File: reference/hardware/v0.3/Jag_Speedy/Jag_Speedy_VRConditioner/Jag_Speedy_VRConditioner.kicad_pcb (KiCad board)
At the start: 2 copper layers, 15 parts, among them IC1 MAX9926UAEE+, J1 Conn_02x04_Counter_Clockwise

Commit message: VR PCB
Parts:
- moved C1 14.9 mm to (149.9, 83.8), turned to 90 degrees
- moved R4 6.02 mm to (144.8, 83.8), turned to 90 degrees
- moved R7 2.21 mm to (141.0, 83.8), turned to 90 degrees
- turned R3 to 270 degrees
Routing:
- net Net-(C1-Pad2): track 36.7 -> 22.3 mm
- net Net-(C1-Pad1): track 24.5 -> 11.3 mm
- net VR1+: track 9.36 -> 18.2 mm
- net VR1-: track 9.19 -> 17.1 mm

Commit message: VR Cond PCB update
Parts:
- J1: value Conn_02x04_Counter_Clockwise -> Conn; moved to B.Cu
- moved C2 26.1 mm to (151.1, 82.9), turned to 90 degrees
- moved R5 20.4 mm to (146.1, 82.9), turned to 270 degrees
- moved R6 19.7 mm to (148.6, 82.9), turned to 90 degrees
- moved R8 18.9 mm to (135.9, 82.9), turned to 90 degrees
- moved C5 18.0 mm to (133.3, 96.9), turned to 90 degrees
- moved R2 15.8 mm to (143.5, 96.9), turned to 270 degrees
- moved C4 14.3 mm to (135.9, 96.9), turned to 90 degrees
- moved R1 14.1 mm to (141.0, 96.9), turned to 270 degrees
- moved R4 11.5 mm to (133.3, 82.9)
- moved C3 11.1 mm to (138.4, 96.9), turned to 90 degrees
- moved IC1 10.4 mm to (148.6, 90.2), turned to 90 degrees
- moved C1 6.42 mm to (143.5, 82.9)
- moved R3 6.09 mm to (141.0, 82.9)
- moved R7 2.71 mm to (138.4, 82.9)
- moved J1 1.98 mm to (134.6, 88.9), turned to 270 degrees
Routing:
- net Ground: track 22.7 -> 56.8 mm
- net VR2-: track 24.3 -> 46.3 mm, vias 0 -> 2
- net VR2+: track 4.66 -> 20.6 mm, vias 0 -> 1
- net Output1: track 35.1 -> 22.5 mm
- net Net-(C2-Pad1): track 0.00 -> 9.84 mm
- net Net-(C2-Pad2): track 0.00 -> 9.09 mm
- net VR1-: track 17.1 -> 10.7 mm, vias 0 -> 2
- net Net-(C1-Pad2): track 22.3 -> 18.1 mm
- net VR1+: track 18.2 -> 22.1 mm
- net 5V: track 32.9 -> 36.5 mm, vias 0 -> 1
- net Net-(C1-Pad1): track 11.3 -> 8.26 mm
- net Output2: track 16.7 -> 15.2 mm
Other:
- net class Power added: clearance 0.3, trace_width 0.25, via_dia 0.8, via_drill 0.4
- board text added: "FiP"

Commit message: PCB Update
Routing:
- net Ground: track 56.8 -> 47.5 mm, vias 0 -> 1
- net VR1+: track 22.1 -> 15.1 mm, vias 0 -> 1
- net VR2-: track 46.3 -> 39.5 mm
- net VR1-: track 10.7 -> 12.3 mm, vias 2 -> 1

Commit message: VR PCB Update
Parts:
- C3, C4, C5, R1, R2: moved to B.Cu
- R7, R8: footprint Resistor_SMD:R_0805_2012Metric -> Resistor_THT:R_Axial_DIN0414_L11.9mm_D4.5mm_P15.24mm_Horizontal
- moved R7 23.2 mm to (156.2, 97.8)
- moved R5 12.7 mm to (133.3, 82.9)
- moved R6 11.7 mm to (136.9, 82.9)
- moved R4 10.7 mm to (144.0, 82.9)
- moved R8 8.90 mm to (127.0, 82.5), turned to 270 degrees
- moved R2 6.48 mm to (149.9, 98.1), turned to 90 degrees
- moved R1 4.62 mm to (145.4, 98.1), turned to 90 degrees
- moved C1 4.06 mm to (147.6, 82.9), turned to 270 degrees
- moved C3 2.84 mm to (141.0, 98.1), turned to 270 degrees
- moved C5 1.80 mm to (132.1, 98.1), turned to 270 degrees
- moved C4 1.42 mm to (136.5, 98.1), turned to 270 degrees
- moved R3 0.51 mm to (140.5, 82.9)
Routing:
- net 5V: track 36.4 -> 61.9 mm
- net VR1+: track 15.1 -> 35.8 mm
- net VR1-: track 12.3 -> 32.7 mm
- net Ground: track 47.5 -> 67.1 mm
- net Net-(C2-Pad1): track 9.84 -> 28.4 mm
- net Net-(C2-Pad2): track 9.09 -> 25.3 mm, vias 0 -> 2
- net VR2-: track 39.5 -> 26.7 mm, vias 2 -> 0
- net Net-(C1-Pad2): track 18.1 -> 11.8 mm
- net Output1: track 22.5 -> 16.4 mm, vias 0 -> 1
- net Net-(C1-Pad1): track 8.26 -> 13.6 mm
- net VR2+: track 20.6 -> 16.4 mm
- net Output2: track 15.2 -> 17.7 mm, vias 0 -> 1

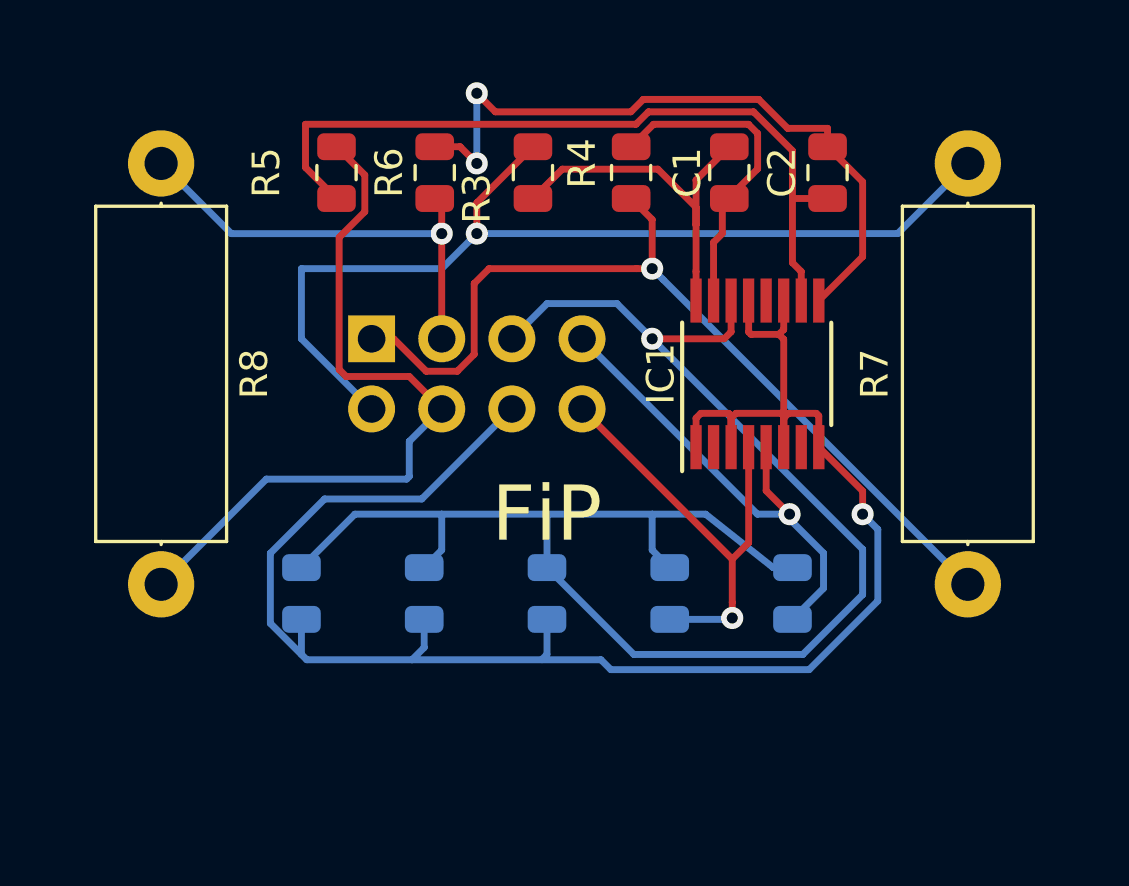
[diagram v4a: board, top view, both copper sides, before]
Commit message: Ground & Pwer Planes
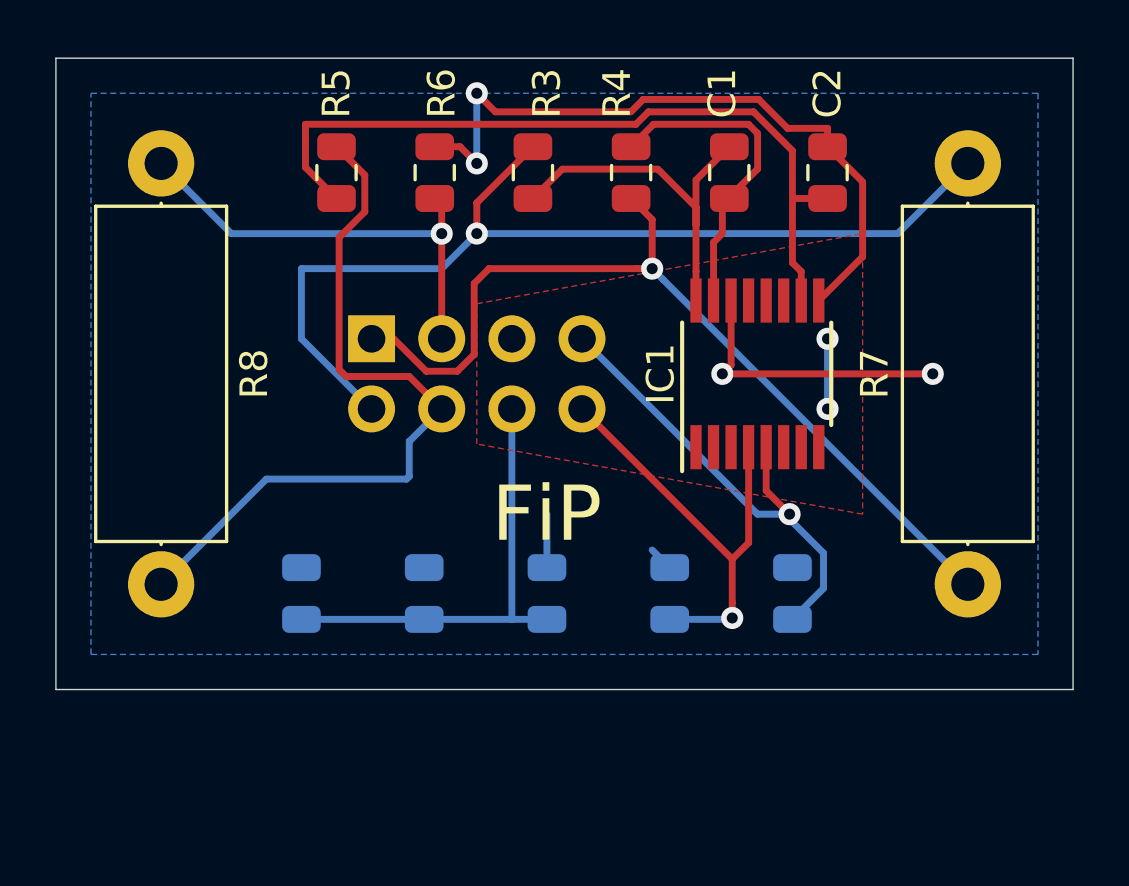
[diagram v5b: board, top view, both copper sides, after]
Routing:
- net 5V: track 61.9 -> 13.2 mm, vias 1 -> 2
- net Ground: track 67.1 -> 19.0 mm, vias 1 -> 2
- added copper zone on B.Cu, net 5V
- added copper zone on F.Cu, net Ground
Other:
- board outline added: 36.8 x 22.9 mm
- net class Power: clearance 0.3 -> 0.2
- net class Signal added: clearance 0.1, trace_width 0.2, via_dia 0.6, via_drill 0.4

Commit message: PCB Connector Fix
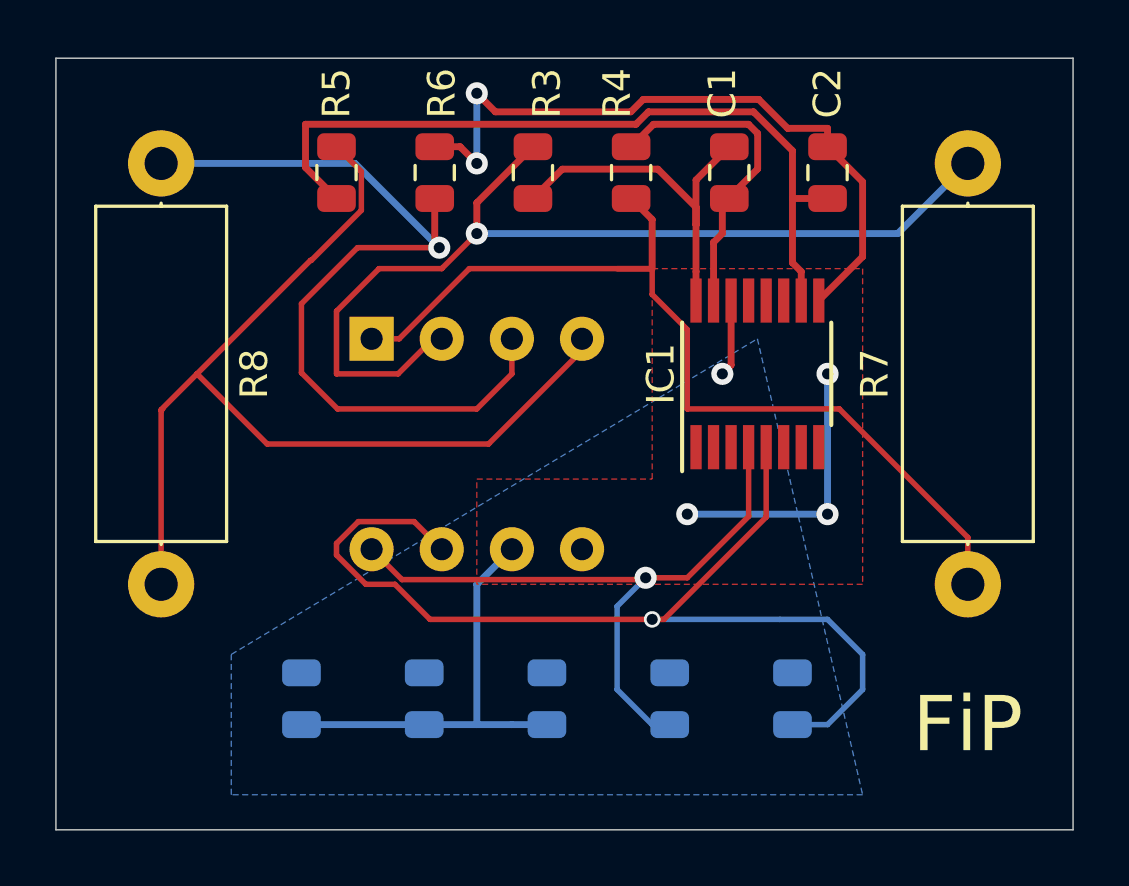
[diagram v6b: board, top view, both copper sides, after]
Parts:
- J1: footprint Connector_PinHeader_2.54mm:PinHeader_2x04_P2.54mm_Vertical -> Package_DIP:DIP-8_W7.62mm_Socket
- moved C3 3.81 mm to (141.0, 101.9)
- moved C4 3.81 mm to (136.5, 101.9)
- moved C5 3.81 mm to (132.1, 101.9)
- moved R1 3.81 mm to (145.4, 101.9)
- moved R2 3.81 mm to (149.9, 101.9)
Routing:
- net Output2: track 17.7 -> 38.0 mm
- net VR2+: track 16.4 -> 31.5 mm
- net 5V: track 13.2 -> 2.79 mm, vias 2 -> 1
- net VR2-: track 26.7 -> 36.2 mm
- net Output1: track 16.4 -> 24.5 mm
- net Ground: track 19.0 -> 25.9 mm, vias 2 -> 3
- net VR1-: track 32.7 -> 34.7 mm, vias 1 -> 0
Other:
- board size 36.8 x 22.9 mm -> 36.8 x 27.9 mm

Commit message: PCB Changes
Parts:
- moved C5 25.0 mm to (156.2, 95.2), turned to 180 degrees
- moved C4 21.7 mm to (156.2, 92.7), turned to 180 degrees
- moved C3 19.3 mm to (156.2, 90.2), turned to 180 degrees
- moved R2 18.0 mm to (156.2, 85.1), turned to 0 degrees
- moved R1 17.9 mm to (156.2, 87.6), turned to 0 degrees
- moved R8 1.27 mm to (128.3, 82.5)
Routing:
- net Output1: track 24.5 -> 45.2 mm
- net Output2: track 38.0 -> 48.5 mm
- net Ground: track 25.9 -> 16.8 mm
- net VR2+: track 31.5 -> 26.5 mm, vias 1 -> 0
- net Net-(C2-Pad1): track 28.4 -> 25.0 mm
- net VR2-: track 36.2 -> 38.5 mm
- net Net-(C2-Pad2): track 25.3 -> 26.1 mm
- net VR1-: track 34.7 -> 35.3 mm
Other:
- board size 36.8 x 27.9 mm -> 35.6 x 22.9 mm

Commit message: PCB Updates
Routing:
- net VR1-: track 35.3 -> 34.2 mm
